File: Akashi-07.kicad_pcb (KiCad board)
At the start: 2 copper layers, 46 parts, among them J1 Conn_Coaxial, J2 Screw_Terminal_01x02, J3 SJ1-3533, J4 Conn_01x08, J5 Conn_01x06, J6 Conn_01x10, J7 Conn_01x08, SW1 SW_Push, U1 Si5351A-B-GT, U2 SN74LVC74APW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

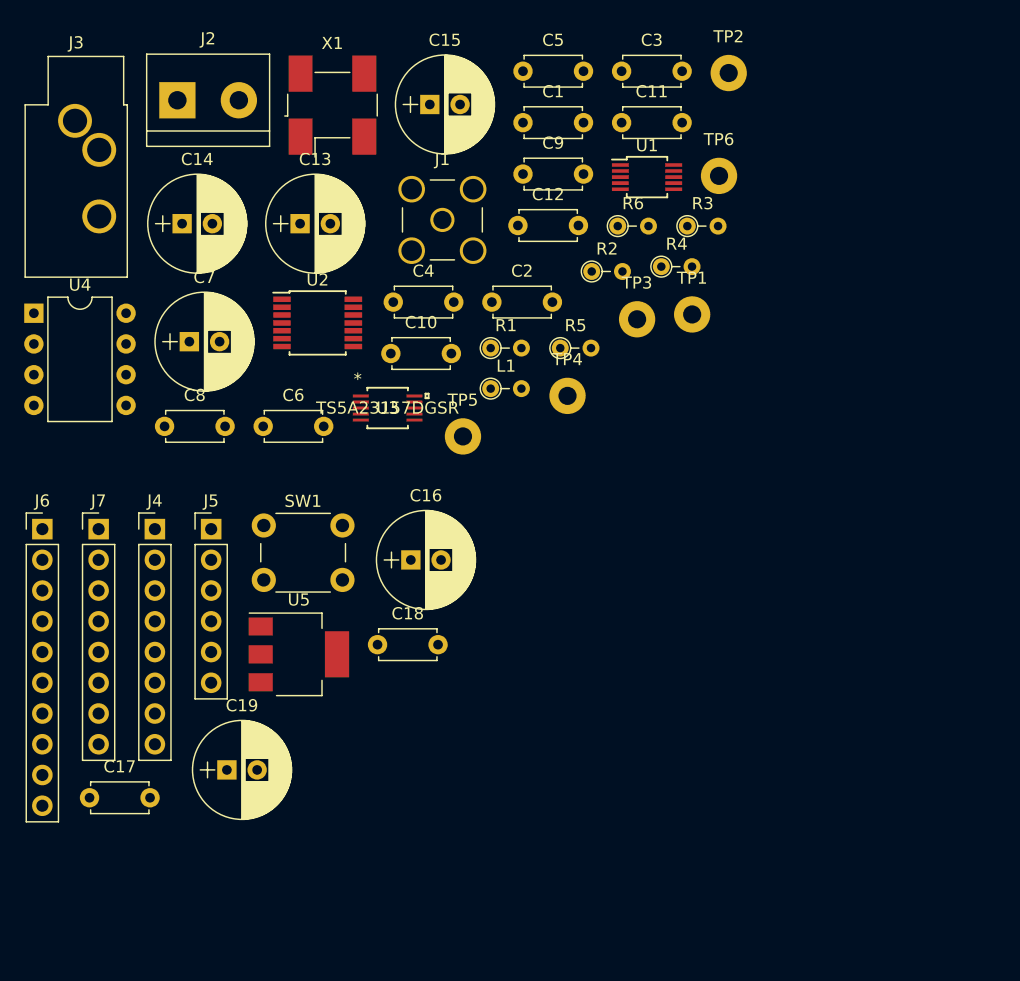
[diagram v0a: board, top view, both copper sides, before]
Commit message: All parts is on the PCB.
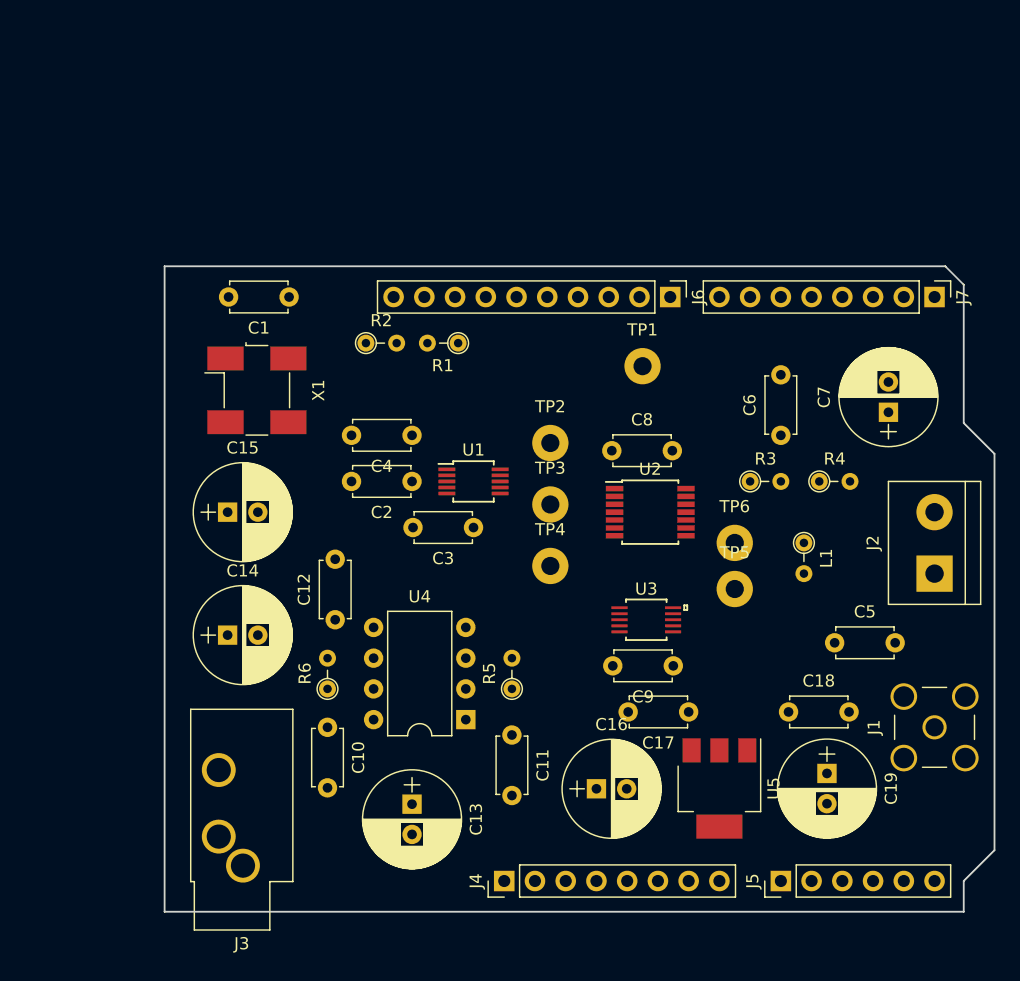
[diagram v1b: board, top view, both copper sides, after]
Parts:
- removed SW1: SW_Push, Buttons_Switches_THT:SW_PUSH_6mm_h5mm
- C10: value 0.01u -> 0.1u
- C12: value 0.1u -> 0.01u
- moved J2 73.8 mm to (175.3, 96.5), turned to 90 degrees
- moved J7 71.7 mm to (175.3, 73.7), turned to 270 degrees
- moved J3 63.1 mm to (118.1, 120.7), turned to 180 degrees
- moved J1 58.4 mm to (175.3, 109.2), turned to 90 degrees
- moved C7 58.1 mm to (171.4, 83.2), turned to 90 degrees
- moved J5 55.3 mm to (162.6, 121.9), turned to 90 degrees
- moved J6 55.3 mm to (153.4, 73.7), turned to 270 degrees
- moved C5 53.8 mm to (167.0, 102.2)
- moved C11 51.4 mm to (140.3, 109.9), turned to 270 degrees
- moved C17 50.0 mm to (154.9, 108.0), turned to 180 degrees
- moved C19 49.6 mm to (166.4, 113.0), turned to 270 degrees
- moved U4 49.0 mm to (136.5, 108.6), turned to 180 degrees
- moved C13 48.9 mm to (132.1, 115.6), turned to 270 degrees
- moved R6 45.1 mm to (125.1, 106.0), turned to 90 degrees
- moved C6 42.8 mm to (162.6, 85.1), turned to 90 degrees
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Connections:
- C10 pad 1: Net-(C10-Pad1) -> VDD
- C12 pad 1: VDD -> Net-(C12-Pad1)
- C14 pad 1: Net-(C10-Pad1) -> Net-(C11-Pad1)
- C15 pad 1: Net-(C11-Pad1) -> Net-(C12-Pad1)
- J3 pad R: (no net) -> GND
- J4 pad 1: Net-(J4-Pad1) -> (no net)
- J4 pad 2: Net-(J4-Pad2) -> (no net)
- J4 pad 3: Net-(J4-Pad3) -> (no net)
- J4 pad 4: Net-(J4-Pad4) -> (no net)
- J4 pad 8: Net-(J4-Pad8) -> (no net)
- J5 pad 1: Net-(J5-Pad1) -> (no net)
- J5 pad 2: Net-(J5-Pad2) -> (no net)
- J5 pad 3: Net-(J5-Pad3) -> (no net)
- J5 pad 4: Net-(J5-Pad4) -> (no net)
- J5 pad 5: Net-(J5-Pad5) -> (no net)
- J5 pad 6: Net-(J5-Pad6) -> (no net)
- J6 pad 1: Net-(J6-Pad1) -> (no net)
- J6 pad 2: Net-(J6-Pad2) -> (no net)
- J6 pad 3: Net-(J6-Pad3) -> (no net)
- J6 pad 4: Net-(J6-Pad4) -> (no net)
- J6 pad 6: Net-(J6-Pad6) -> (no net)
- J6 pad 8: Net-(J6-Pad8) -> (no net)
- J7 pad 1: Net-(J7-Pad1) -> (no net)
- J7 pad 2: Net-(J7-Pad2) -> (no net)
- J7 pad 3: Net-(J7-Pad3) -> (no net)
- J7 pad 4: Net-(J7-Pad4) -> (no net)
- J7 pad 5: Net-(J7-Pad5) -> (no net)
- J7 pad 6: Net-(J7-Pad6) -> (no net)
- J7 pad 7: Net-(J7-Pad7) -> (no net)
- J7 pad 8: Net-(J7-Pad8) -> (no net)
- R5 pad 1: Net-(C10-Pad1) -> Net-(C11-Pad1)
- R6 pad 1: Net-(C11-Pad1) -> Net-(C12-Pad1)
- TP1 pad 1: Net-(C2-Pad2) -> GND
- TP2 pad 1: /connector/SCL -> Net-(TP2-Pad1)
- TP3 pad 1: /connector/SDA -> Net-(TP3-Pad1)
- U1 pad 10: Net-(TP4-Pad1) -> Net-(TP2-Pad1)
- U1 pad 3: Net-(U1-Pad3) -> (no net)
- U1 pad 6: Net-(U1-Pad6) -> Net-(TP4-Pad1)
- U1 pad 9: Net-(U1-Pad9) -> Net-(TP3-Pad1)
- U2 pad 11: Net-(TP4-Pad1) -> Net-(TP2-Pad1)
- U2 pad 3: Net-(TP4-Pad1) -> Net-(TP2-Pad1)
- U2 pad 6: Net-(U2-Pad6) -> (no net)
- U4 pad 1: Net-(C10-Pad1) -> Net-(C11-Pad1)
- U4 pad 2: Net-(C10-Pad1) -> Net-(C11-Pad1)
- U4 pad 6: Net-(C11-Pad1) -> Net-(C12-Pad1)
- U4 pad 7: Net-(C11-Pad1) -> Net-(C12-Pad1)
- X1 pad 1: Net-(X1-Pad1) -> (no net)
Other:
- board outline added: 68.6 x 53.3 mm

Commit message: Refined symbol names
Adjust the position.
Added copyright and board name.
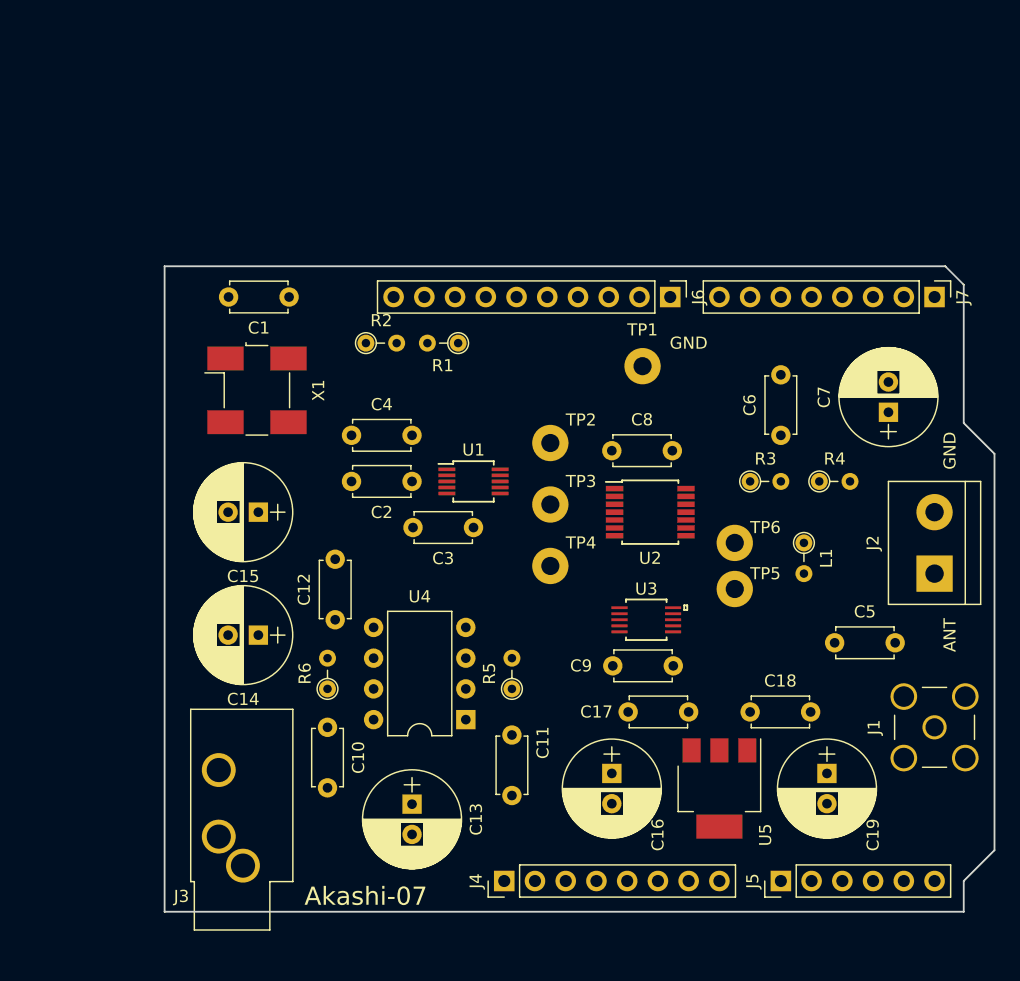
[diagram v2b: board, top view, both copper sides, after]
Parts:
- moved C18 3.17 mm to (160.0, 108.0)
- moved C14 2.54 mm to (119.4, 101.6), turned to 180 degrees
- moved C15 2.54 mm to (119.4, 91.4), turned to 180 degrees
- moved C16 1.80 mm to (148.6, 113.0), turned to 270 degrees
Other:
- board text added: "ANT"
- board text added: "Akashi-07"
- board text added: "Akashi-07 : (C) 2020 Seiichi Horie https://github.com/suikan4github/Akashi-07"
- board text added: "GND"

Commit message: Routing finished.
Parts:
- moved C1 1.27 mm to (121.9, 74.9)
- moved C5 0.64 mm to (167.0, 102.9)
- moved U3 0.17 mm to (151.4, 100.5)
- moved U1 0.10 mm to (137.2, 89.0)
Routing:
- net VDD: track 0.00 -> 170.1 mm, vias 0 -> 3
- net Net-(C6-Pad1): track 0.00 -> 69.9 mm, vias 0 -> 2
- net Net-(TP2-Pad1): track 0.00 -> 45.7 mm, vias 0 -> 2
- net /connector/SCL: track 0.00 -> 38.2 mm
- net Net-(C11-Pad1): track 0.00 -> 30.8 mm
- net Net-(C15-Pad2): track 0.00 -> 29.7 mm
- net Net-(R6-Pad2): track 0.00 -> 25.9 mm
- net Net-(C5-Pad1): track 0.00 -> 25.7 mm
- net Net-(TP5-Pad1): track 0.00 -> 24.7 mm, vias 0 -> 2
- net Net-(C12-Pad1): track 0.00 -> 22.4 mm
- net /connector/SDA: track 0.00 -> 21.2 mm
- net Net-(C16-Pad1): track 0.00 -> 19.5 mm
- net Net-(C14-Pad2): track 0.00 -> 18.4 mm
- net Net-(C5-Pad2): track 0.00 -> 15.4 mm
- net GND: track 0.00 -> 13.8 mm, vias 0 -> 7
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- added copper zone on B.Cu, net GND
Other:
- board text added: "Q1"
- board text added: "Q2"

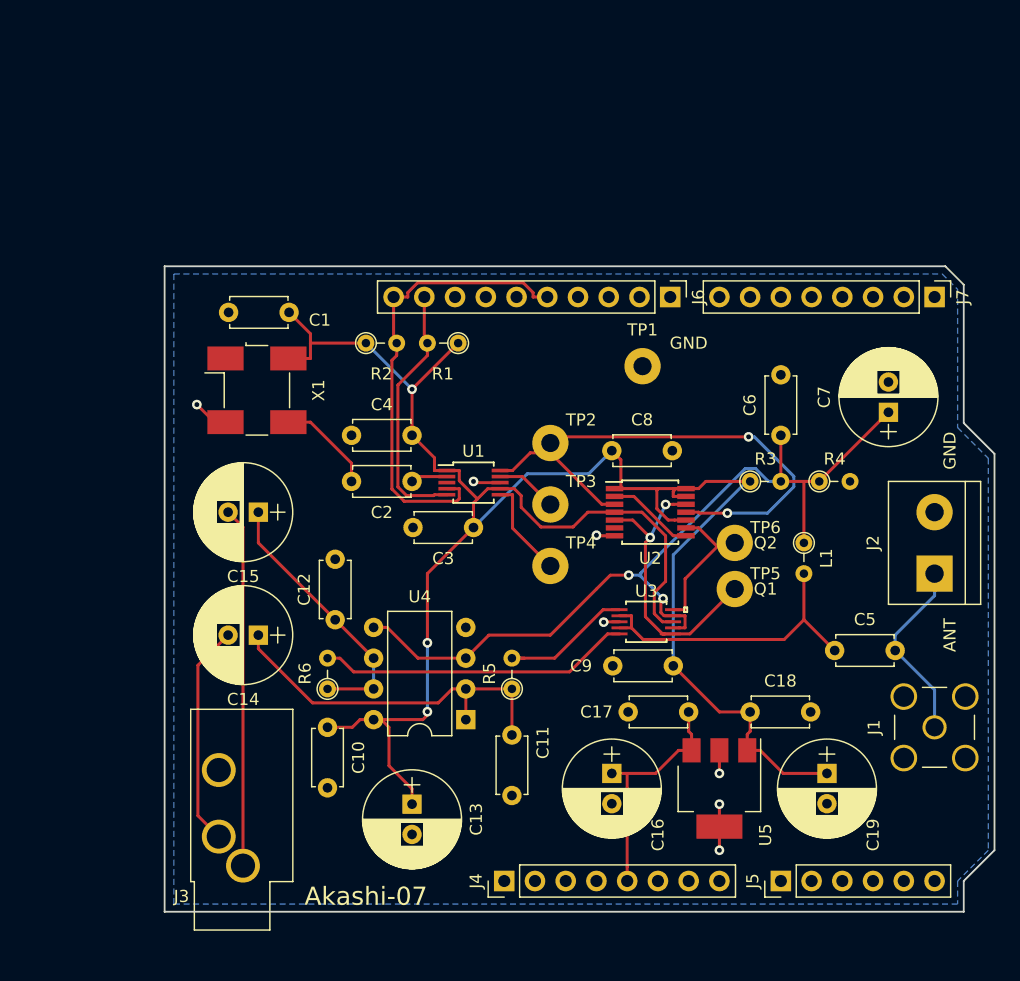
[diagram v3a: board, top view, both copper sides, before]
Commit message: Added jumper to short the op-amp.
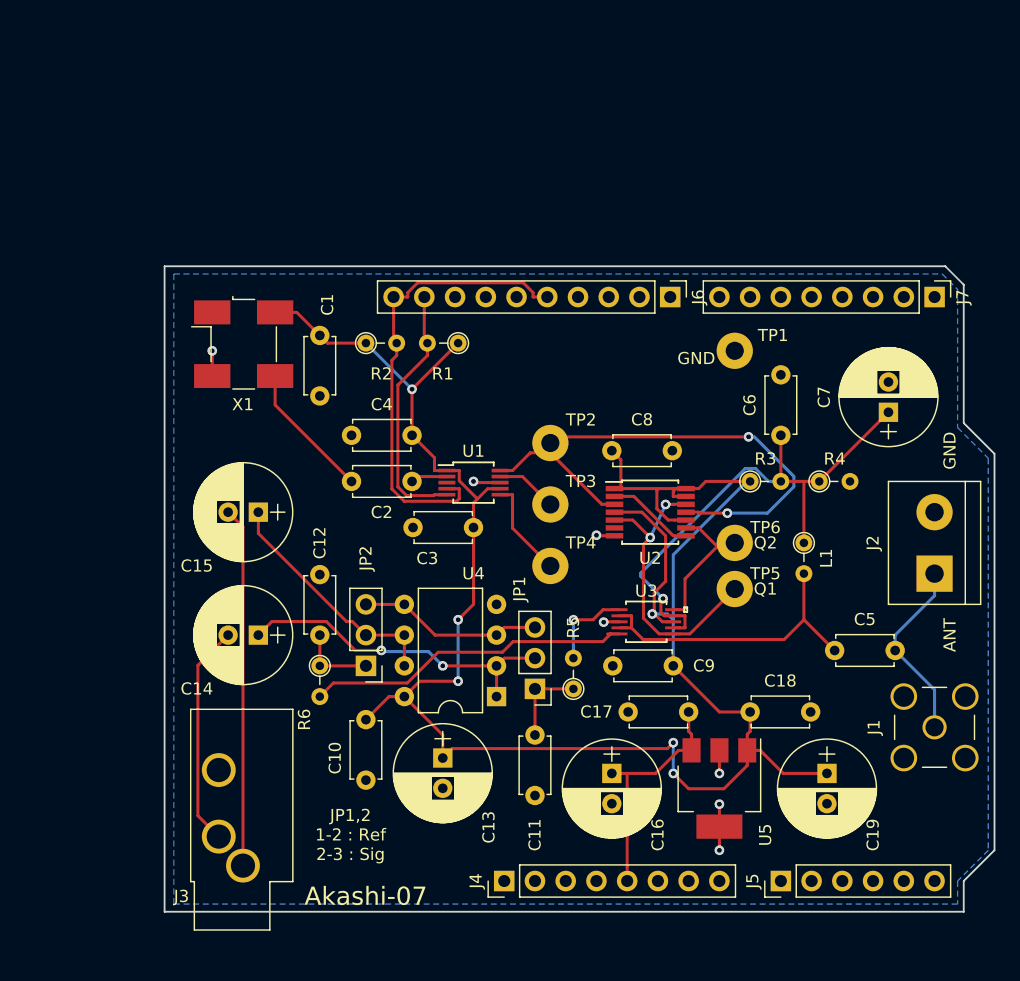
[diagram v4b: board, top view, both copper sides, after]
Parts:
- added JP1: Jumper_3_Open, Pin_Headers:Pin_Header_Straight_1x03_Pitch2.54mm, F.Cu at (142.2, 106.0)
- added JP2: Jumper_3_Open, Pin_Headers:Pin_Header_Straight_1x03_Pitch2.54mm, F.Cu at (128.3, 104.1)
- moved TP1 7.73 mm to (158.8, 78.1)
- moved R5 5.08 mm to (145.4, 106.0)
- moved C13 4.58 mm to (134.6, 111.8)
- moved X1 3.96 mm to (118.2, 77.6)
- moved C10 3.24 mm to (128.3, 108.6)
- moved C1 3.17 mm to (124.5, 76.8), turned to 270 degrees
- moved U4 3.17 mm to (139.1, 106.7)
- moved R6 2.01 mm to (124.5, 104.1), turned to 270 degrees
- moved C11 1.91 mm to (142.2, 109.9)
- moved C12 1.80 mm to (124.5, 101.6)
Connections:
- C14 pad 1: Net-(C11-Pad1) -> Net-(C14-Pad1)
- C15 pad 1: Net-(C12-Pad1) -> Net-(C15-Pad1)
- J4 pad 1: (no net) -> Net-(J4-Pad1)
- J4 pad 2: (no net) -> Net-(J4-Pad2)
- J4 pad 3: (no net) -> Net-(J4-Pad3)
- J4 pad 4: (no net) -> Net-(J4-Pad4)
- J4 pad 8: (no net) -> Net-(J4-Pad8)
- J5 pad 1: (no net) -> Net-(J5-Pad1)
- J5 pad 2: (no net) -> Net-(J5-Pad2)
- J5 pad 3: (no net) -> Net-(J5-Pad3)
- J5 pad 4: (no net) -> Net-(J5-Pad4)
- J5 pad 5: (no net) -> Net-(J5-Pad5)
- J5 pad 6: (no net) -> Net-(J5-Pad6)
- J6 pad 1: (no net) -> Net-(J6-Pad1)
- J6 pad 2: (no net) -> Net-(J6-Pad2)
- J6 pad 3: (no net) -> Net-(J6-Pad3)
- J6 pad 4: (no net) -> Net-(J6-Pad4)
- J6 pad 6: (no net) -> Net-(J6-Pad6)
- J6 pad 8: (no net) -> Net-(J6-Pad8)
- J7 pad 1: (no net) -> Net-(J7-Pad1)
- J7 pad 2: (no net) -> Net-(J7-Pad2)
- J7 pad 3: (no net) -> Net-(J7-Pad3)
- J7 pad 4: (no net) -> Net-(J7-Pad4)
- J7 pad 5: (no net) -> Net-(J7-Pad5)
- J7 pad 6: (no net) -> Net-(J7-Pad6)
- J7 pad 7: (no net) -> Net-(J7-Pad7)
- J7 pad 8: (no net) -> Net-(J7-Pad8)
- U1 pad 3: (no net) -> Net-(U1-Pad3)
- U2 pad 6: (no net) -> Net-(U2-Pad6)
- U4 pad 1: Net-(C11-Pad1) -> Net-(C14-Pad1)
- U4 pad 2: Net-(C11-Pad1) -> Net-(C14-Pad1)
- U4 pad 3: Net-(C6-Pad1) -> Net-(JP1-Pad3)
- U4 pad 5: Net-(C6-Pad1) -> Net-(JP1-Pad3)
- U4 pad 6: Net-(C12-Pad1) -> Net-(C15-Pad1)
- U4 pad 7: Net-(C12-Pad1) -> Net-(C15-Pad1)
- X1 pad 1: (no net) -> Net-(X1-Pad1)
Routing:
- net Net-(C14-Pad1): track 0.00 -> 27.6 mm, vias 0 -> 2
- net Net-(C6-Pad1): track 69.9 -> 43.9 mm, vias 2 -> 1
- net Net-(C11-Pad1): track 30.8 -> 6.98 mm
- net Net-(C15-Pad1): track 0.00 -> 19.8 mm
- net Net-(C12-Pad1): track 22.4 -> 6.35 mm
- net Net-(JP1-Pad3): track 0.00 -> 15.3 mm
- net Net-(R5-Pad2): track 11.6 -> 7.33 mm, vias 0 -> 1
- net Net-(C2-Pad2): track 8.13 -> 11.3 mm
- net Net-(R6-Pad2): track 25.9 -> 27.2 mm
- net GND: track 13.8 -> 12.9 mm
- net VDD: track 170.1 -> 169.5 mm, vias 3 -> 6
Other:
- board text added: "JP1,2 1-2 : Ref 2-3 : Sig"

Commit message: Change TA48L033F foot print
Added VDD plane on the FC layer.
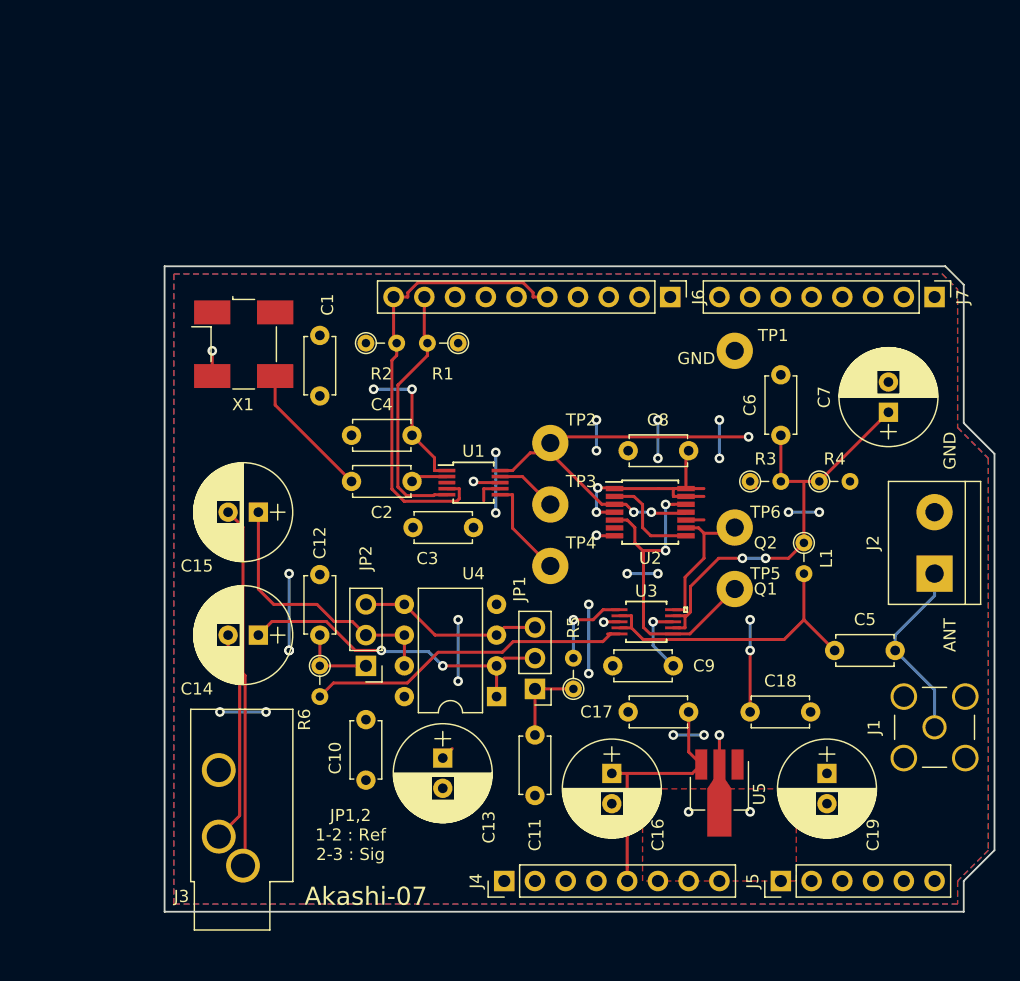
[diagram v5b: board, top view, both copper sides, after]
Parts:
- U5: footprint TO_SOT_Packages_SMD:SOT-223-3_TabPin2 -> TO_SOT_Packages_SMD:SOT-89-3_Handsoldering
- moved C8 6.35 mm to (154.9, 86.4), turned to 180 degrees
- moved TP6 1.27 mm to (158.8, 92.7)
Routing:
- net VDD: track 169.5 -> 86.5 mm, vias 6 -> 28
- net Net-(TP2-Pad1): track 45.7 -> 36.2 mm, vias 2 -> 3
- net Net-(C6-Pad1): track 43.9 -> 36.6 mm, vias 1 -> 2
- net (no net): track 0.00 -> 5.72 mm, vias 0 -> 2
- net GND: track 12.9 -> 17.2 mm
- net Net-(C15-Pad1): track 19.8 -> 22.5 mm
- net Net-(TP5-Pad1): track 24.8 -> 27.2 mm
- net Net-(C16-Pad1): track 19.5 -> 21.4 mm
- net Net-(U2-Pad2): track 7.25 -> 8.35 mm
- net Net-(C14-Pad2): track 18.4 -> 17.8 mm
- added copper zone on F.Cu, net GND
- added copper zone on F.Cu, net VDD

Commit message: BOM is ready
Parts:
- moved C13 1.31 mm to (134.6, 113.1)
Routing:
- net VDD: track 86.5 -> 85.4 mm
